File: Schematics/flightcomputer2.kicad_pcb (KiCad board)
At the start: 2 copper layers, 42 parts, among them IC1 AMS1117-3.3, J1 Pyro, J2 USB_C_Receptacle, J3 Conn_01x05_Pin, J4 Conn_Coaxial_Small, J5 Conn_01x05_Pin, J6 PyroDrogue, Q1 BSC098N10NS5, Q2 BSC098N10NS5, SW3 SW_Push, SW4 SW_Push, U2 STM32F405RGTx, U4 SN65HVD230DR

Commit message: added LCSC numbers and footprint values, need to connect schemeatic pins, then can start layout
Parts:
- removed IC1: AMS1117-3.3, Library:SOT229P700X180-4N
- removed SW3, SW4: SW_Push, Library:SAMZO G4R0015010
- added BootSwitch1: SAMZO G4R0015010, myFootprints:SAMZO G4R0015010, F.Cu at (274.1, 76.5)
- added C1: 100nf, Capacitor_SMD:C_0805_2012Metric_Pad1.18x1.45mm_HandSolder, F.Cu at (242.4, 142.0)
- added C10: 100nf, Capacitor_SMD:C_0805_2012Metric_Pad1.18x1.45mm_HandSolder, F.Cu at (42.9, 40.8)
- added C11: 100nf, Capacitor_SMD:C_0805_2012Metric_Pad1.18x1.45mm_HandSolder, F.Cu at (45.9, 40.8)
- added C12: 1u, Capacitor_SMD:C_0805_2012Metric_Pad1.18x1.45mm_HandSolder, F.Cu at (48.9, 40.8)
- added C14: 18p, Capacitor_SMD:C_0603_1608Metric_Pad1.08x0.95mm_HandSolder, F.Cu at (42.6, 75.7)
- added C16: 100nf, Capacitor_SMD:C_0805_2012Metric_Pad1.18x1.45mm_HandSolder, F.Cu at (206.3, 124.1)
- added C17: 1u, Capacitor_SMD:C_0805_2012Metric_Pad1.18x1.45mm_HandSolder, F.Cu at (97.6, 99.7)
- added C18: 33u, Capacitor_SMD:C_0805_2012Metric_Pad1.18x1.45mm_HandSolder, F.Cu at (97.6, 102.7)
- added C19: 100nf, Capacitor_SMD:C_0805_2012Metric_Pad1.18x1.45mm_HandSolder, F.Cu at (32.1, 119.1)
- added C21: 100nf, Capacitor_SMD:C_0805_2012Metric_Pad1.18x1.45mm_HandSolder, F.Cu at (28.8, 126.5)
- added C22: 100nf, Capacitor_SMD:C_0805_2012Metric_Pad1.18x1.45mm_HandSolder, F.Cu at (30.4, 48.6)
- added C23: 100nf, Capacitor_SMD:C_0805_2012Metric_Pad1.18x1.45mm_HandSolder, F.Cu at (30.4, 51.6)
- added C7: 100nf, Capacitor_SMD:C_0805_2012Metric_Pad1.18x1.45mm_HandSolder, F.Cu at (39.9, 40.8)
- added CAN_IN1: CAN, myFootprints:MOLEX_26013114, F.Cu at (19.2, 144.3)
- added CAN_OUT1: CAN, myFootprints:MOLEX_26013114, F.Cu at (28.6, 144.3)
- added D1: NeoPixel_THT, LED_SMD:LED_Kingbright_AAA3528ESGCT, F.Cu at (261.3, 148.6)
- added D3: SRV05-4.TCT, myFootprints:SOT95P280X145-6N, F.Cu at (213.8, 32.2)
- added J1: Microsemi_FlashPro-JTAG-10, myFootprints:CONN_7024610XX_MOL, F.Cu at (82.2, 34.7)
- added J7: Conn_Coaxial_Small, Connector_Coaxial:SMA_Amphenol_132291_Vertical, F.Cu at (137.4, 29.8)
- added J8: Micro_SD_Card, Connector_Card:microSD_HC_Molex_104031-0811, F.Cu at (199.7, 27.2)
- added JP1: SolderJumper_2_Open, Jumper:SolderJumper-2_P1.3mm_Open_TrianglePad1.0x1.5mm, F.Cu at (207.8, 128.9)
- added MPL3115A2R1: MPL3115A2R1, myFootprints:PSON80P300X300X100-8N, F.Cu at (36.8, 120.7)
- added PowerLED1: RLED, LED_SMD:LED_0603_1608Metric_Pad1.05x0.95mm_HandSolder, F.Cu at (263.1, 107.3)
- added R1: 10k, Resistor_SMD:R_0805_2012Metric_Pad1.20x1.40mm_HandSolder, F.Cu at (258.6, 41.5)
- added R16: 10k, Resistor_SMD:R_0805_2012Metric_Pad1.20x1.40mm_HandSolder, F.Cu at (200.7, 38.3)
- added R17: 220R, Resistor_SMD:R_0805_2012Metric_Pad1.20x1.40mm_HandSolder, F.Cu at (203.6, 38.3)
- added R2: 100k, Resistor_SMD:R_0805_2012Metric_Pad1.20x1.40mm_HandSolder, F.Cu at (267.2, 78.1)
- added R3: 1k, Resistor_SMD:R_0805_2012Metric_Pad1.20x1.40mm_HandSolder, F.Cu at (258.5, 102.0)
- added R4: 330R, Resistor_SMD:R_0805_2012Metric_Pad1.20x1.40mm_HandSolder, F.Cu at (247.2, 150.8)
- added R9: 120R, Resistor_SMD:R_0805_2012Metric_Pad1.20x1.40mm_HandSolder, F.Cu at (212.0, 124.2)
- added RSTSwitch1: SAMZO G4R0015010, myFootprints:SAMZO G4R0015010, F.Cu at (265.5, 48.5)
- added U2: SN65HVD230, Package_SO:SOIC-8_3.9x4.9mm_P1.27mm, F.Cu at (211.8, 118.0)
- added U3: AMS1117-3.3, Package_TO_SOT_SMD:SOT-223-3_TabPin2, F.Cu at (100.1, 94.1)
- added U5: H3LIS100DL, myFootprints:PQFN50P300X300X100-16N, F.Cu at (30.1, 91.7)
- added Y1: 8mhz, Crystal:Crystal_SMD_3225-4Pin_3.2x2.5mm_HandSoldering, F.Cu at (33.3, 67.0)
- C15: value 100nf -> 18p; footprint Capacitor_SMD:C_0805_2012Metric_Pad1.18x1.45mm_HandSolder -> Capacitor_SMD:C_0603_1608Metric_Pad1.08x0.95mm_HandSolder
- C9: renamed from C12; value 10u -> 100nf
- D2: footprint Library:SOT95P280X145-6N -> myFootprints:SOT95P280X145-6N
- J2: renamed from J6; value PyroDrogue -> Pyro; footprint Connector_Molex:Molex_KK-254_AE-6410-02A_1x02_P2.54mm_Vertical -> myFootprints:MOLEX_26013114
- J4: renamed from J1; footprint Connector_Molex:Molex_KK-254_AE-6410-02A_1x02_P2.54mm_Vertical -> myFootprints:MOLEX_26013114
- Q1: renamed from Q2; footprint Package_TO_SOT_SMD:SOT-23 -> Package_TO_SOT_SMD:SOT-23-5
- Q2: renamed from Q1; footprint Package_TO_SOT_SMD:SOT-23 -> Package_TO_SOT_SMD:SOT-23-5
- R12: renamed from R9; footprint Resistor_SMD:R_0805_2012Metric -> Resistor_SMD:R_0805_2012Metric_Pad1.20x1.40mm_HandSolder
- R7: renamed from R11; footprint Resistor_SMD:R_0805_2012Metric -> Resistor_SMD:R_0805_2012Metric_Pad1.20x1.40mm_HandSolder
- U1: renamed from U2; value STM32F405RGTx -> STM32F405RGT6
- U4: value SN65HVD230DR -> LSM6DS3TR-C; footprint Library:SOIC127P599X175-8N -> myFootprints:LGA-14-2.5X3MM
- moved R6 188.3 mm to (52.1, 169.0)
- moved R6 188.3 mm to (59.4, 157.5)
- moved R7 188.3 mm to (59.4, 148.7)
- moved R5 188.3 mm to (59.4, 154.6)
- moved R5 188.3 mm to (52.1, 166.1)
- moved R7 188.3 mm to (59.5, 173.0)
- moved R8 188.3 mm to (59.4, 151.6)
- moved R8 188.3 mm to (59.5, 185.2)
- moved R10 177.2 mm to (115.4, 174.4)
- moved R11 177.2 mm to (115.4, 177.3)
- moved R13 177.2 mm to (115.4, 183.2)
- moved R12 177.2 mm to (115.4, 180.3)
- moved C20 175.8 mm to (33.6, 126.9)
- moved C15 158.4 mm to (27.9, 75.1)
- moved C13 155.7 mm to (34.0, 25.1)
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- renumbered C17 to C13, C3 to C2, C13 to C3, C14 to C4, C18 to C5, C19 to C6, C11 to C8, FB2 to FB1, J2 to J3, J3 to J5, J5 to J6, R1 to R10, R2 to R11, R10 to R13, R3 to R14, R4 to R15, R13 to R5, R14 to R6, R12 to R8
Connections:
- net vbat renamed +BATT
- C13 pad 1: +3.3V -> +3.3VA
- C13 pad 2: GND -> +3.3V
- C15 pad 1: +3.3V -> /MCU/OSC OUT
- C15 pad 2: GND -> +3.3V
- C2 pad 1: /MCU1/NRST -> /MCU/NRST
- C20 pad 2: GND -> +3.3V
- C3 pad 2: GND -> +3.3V
- C4 pad 2: GND -> +3.3V
- C5 pad 2: GND -> +3.3V
- C6 pad 2: GND -> +3.3V
- C8 pad 1: GND -> +3.3V
- C8 pad 2: +3.3VA -> +3.3V
- C9 pad 1: GND -> +3.3V
- CBulk1 pad 2: GND -> +3.3V
- D2 pad 2: GND -> +3.3V
- D2 pad 5: VBUS -> +5V
- J2 pad 2: Net-(J6-Pin_2) -> Net-(J2-Pin_2)
- J3 pad S1: GND -> +3.3V
- J4 pad 2: Net-(J1-Pin_2) -> Net-(J4-Pin_2)
- J5 pad 2: GND -> +3.3V
- J5 pad 4: Net-(J3-Pin_4) -> GPS1_RX
- J6 pad 2: GND -> +3.3V
- J6 pad 4: Net-(J5-Pin_4) -> GPS2_RX
- Q1 pad 1: GND -> +3.3V
- Q1 pad 2: GND -> +3.3V
- Q1 pad 3: GND -> +3.3V
- Q2 pad 1: GND -> +3.3V
- Q2 pad 2: GND -> +3.3V
- Q2 pad 3: GND -> +3.3V
- R10 pad 1: Net-(Q1-G) -> Net-(Q2-G)
- R10 pad 2: PA9 -> /Drogue/DrougeIgnite
- R11 pad 1: Net-(Q1-G) -> Net-(Q2-G)
- R11 pad 2: GND -> +3.3V
- R12 pad 1: Net-(J1-Pin_2) -> Net-(J4-Pin_2)
- R12 pad 2: PA3 -> /Drogue/DrougeACD
- R13 pad 1: PA3 -> /Drogue/DrougeACD
- R13 pad 2: GND -> +3.3V
- R14 pad 2: GND -> +3.3V
- R15 pad 2: GND -> +3.3V
- R5 pad 1: Net-(Q2-G) -> Net-(Q1-G)
- R5 pad 2: PA8 -> /Pyro/PyroIgnite
- R6 pad 1: Net-(Q2-G) -> Net-(Q1-G)
- R6 pad 2: GND -> +3.3V
- R7 pad 1: Net-(J6-Pin_2) -> Net-(J2-Pin_2)
- R7 pad 2: PA3 -> /Pyro/PyroADC
- R8 pad 1: PA3 -> /Pyro/PyroADC
- R8 pad 2: GND -> +3.3V
- U1 pad 10: unconnected-(U2-PC2-Pad10) -> /MCU/SPI2-MISO
- U1 pad 11: unconnected-(U2-PC3-Pad11) -> /MCU/SPI2-MOSI
- U1 pad 12: GND -> +3.3V
- U1 pad 13: +3.3V -> +3.3VA
- U1 pad 15: unconnected-(U2-PA1-Pad15) -> /MCU/PyroADC
- U1 pad 17: PA3 -> unconnected-(U1-PA3-Pad17)
- U1 pad 18: GND -> +3.3V
- U1 pad 24: unconnected-(U2-PC4-Pad24) -> /MCU/RGB_DATA
- U1 pad 25: unconnected-(U2-PC5-Pad25) -> /MCU/DrougeADC
- U1 pad 29: GPS1_TX -> /MCU/GPS1_TX
- U1 pad 30: GPS1_RX -> /MCU/GPS1_RX
- U1 pad 33: CAN_RX_2 -> /MCU/CAN_RX_2
- U1 pad 34: CAN_TX_2 -> /MCU/CAN_TX_2
- U1 pad 37: GPS2_RX -> /MCU/GPS2_RX
- U1 pad 38: GPS2_TX -> /MCU/GPS2_TX
- U1 pad 41: PA8 -> unconnected-(U1-PA8-Pad41)
- U1 pad 42: PA9 -> /MCU/VBUS
- U1 pad 44: D- -> /MCU/D-
- U1 pad 45: D+ -> /MCU/D+
- U1 pad 46: VBUS -> /MCU/SWDIO
- U1 pad 49: unconnected-(U2-PA14-Pad49) -> /MCU/SWCLK
- U1 pad 5: unconnected-(U2-PH0-Pad5) -> /MCU/OSC IN
- U1 pad 53: UART_DEBUG_TX -> unconnected-(U1-PC12-Pad53)
- U1 pad 54: UART_DEBUG_RX -> unconnected-(U1-PD2-Pad54)
- U1 pad 58: unconnected-(U2-PB6-Pad58) -> /MCU/I2CSDA
- U1 pad 59: unconnected-(U2-PB7-Pad59) -> /MCU/I2CSDL
- U1 pad 6: unconnected-(U2-PH1-Pad6) -> /MCU/OSC OUT
- U1 pad 60: /MCU1/BOOT0 -> /MCU/BOOT0
- U1 pad 63: GND -> +3.3V
- U1 pad 7: /MCU1/NRST -> /MCU/NRST
- U4 pad 1: CAN_TX_2 -> +3.3V
- U4 pad 2: GND -> +3.3V
- U4 pad 3: +3V3 -> +3.3V
- U4 pad 4: CAN_RX_2 -> unconnected-(U4-INT1-Pad4)
- U4 pad 5: unconnected-(U4-VREF-Pad5) -> +3.3V
- U4 pad 6: CANL -> +3.3V
- U4 pad 7: CANH -> +3.3V
- U4 pad 8: GND -> +3.3V

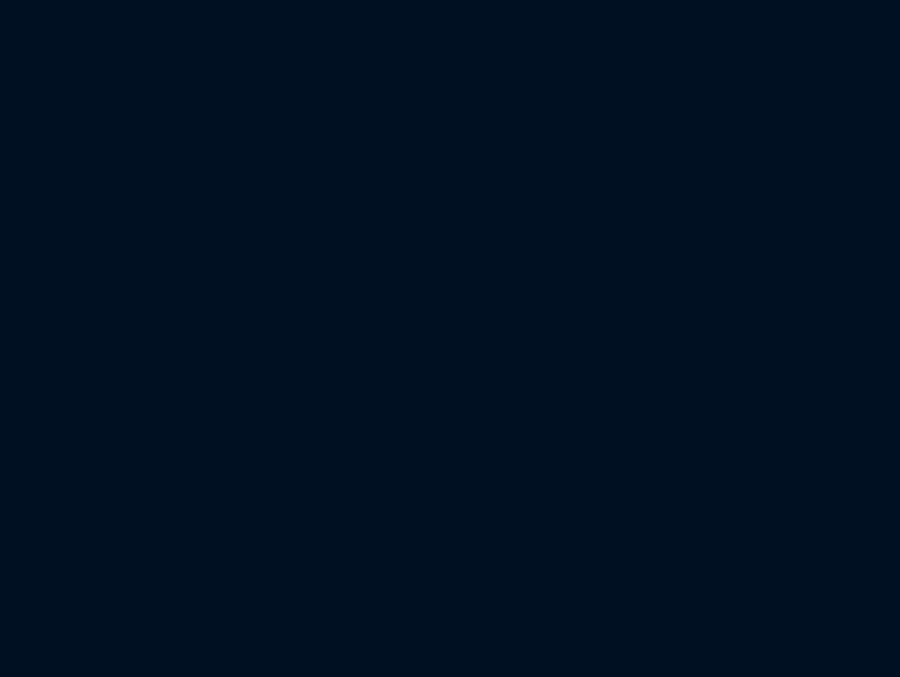
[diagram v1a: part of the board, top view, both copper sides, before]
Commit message: started lora schematic all pcb parts should be included
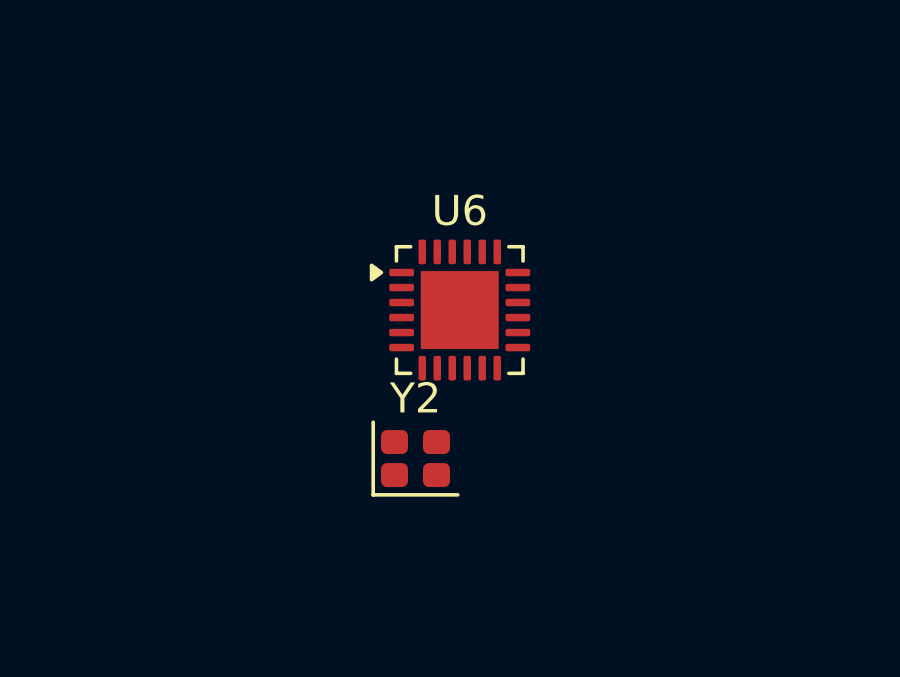
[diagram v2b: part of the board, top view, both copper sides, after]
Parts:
- added U6: SX1262IMLTRT, Package_DFN_QFN:QFN-24-1EP_4x4mm_P0.5mm_EP2.6x2.6mm, F.Cu at (139.1, 118.6)
- added Y2: Crystal_GND24, Crystal:Crystal_SMD_2016-4Pin_2.0x1.6mm, F.Cu at (137.6, 123.5)

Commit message: finished pin assignments and ran ERC all good ready for layout
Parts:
- removed the C2 at (268.2, 39.9)
- removed the C2 at (275.3, 47.0)
- removed CBulk1: 4.7u, Capacitor_SMD:C_0805_2012Metric_Pad1.18x1.45mm_HandSolder
- removed the R4 at (247.2, 150.8)
- removed the R8 at (59.5, 185.2)
- removed the U6 at (139.1, 118.6)
- removed Y2: Crystal_GND24, Crystal:Crystal_SMD_2016-4Pin_2.0x1.6mm
- added C2: 100nf, Capacitor_SMD:C_0805_2012Metric_Pad1.18x1.45mm_HandSolder, F.Cu at (144.9, 96.1)
- added C23: 100nf, Capacitor_SMD:C_0805_2012Metric_Pad1.18x1.45mm_HandSolder, F.Cu at (128.3, 66.5)
- added C26: 100nf, Capacitor_SMD:C_0805_2012Metric_Pad1.18x1.45mm_HandSolder, F.Cu at (105.0, 97.0)
- added C27: 1u, Capacitor_SMD:C_0805_2012Metric_Pad1.18x1.45mm_HandSolder, F.Cu at (105.0, 100.0)
- added C8: 4.7u, Capacitor_SMD:C_0805_2012Metric_Pad1.18x1.45mm_HandSolder, F.Cu at (126.5, 87.6)
- added D2: D_Schottky, Diode_SMD:D_2114_3652Metric, F.Cu at (121.4, 123.3)
- added D3: D_Schottky, Diode_SMD:D_2114_3652Metric, F.Cu at (121.5, 118.5)
- added U4: RFM95W-915S2, myFootprints:XCVR_RFM95W-915S2, F.Cu at (111.0, 139.0)
- C15: renamed from C14; footprint Capacitor_SMD:C_0603_1608Metric_Pad1.08x0.95mm_HandSolder -> Capacitor_SMD:C_0805_2012Metric_Pad1.18x1.45mm_HandSolder
- C16: renamed from C15; footprint Capacitor_SMD:C_0603_1608Metric_Pad1.08x0.95mm_HandSolder -> Capacitor_SMD:C_0805_2012Metric_Pad1.18x1.45mm_HandSolder
- C19: renamed from C18; value 33u -> 4.7u
- J8: footprint Connector_Card:microSD_HC_Molex_104031-0811 -> Connector_Card:microSD_HC_Molex_47219-2001
- U3: value AMS1117-3.3 -> LDL1117-3.3; footprint Package_TO_SOT_SMD:SOT-223-3_TabPin2 -> myFootprints:SOT230P700X180-4N
- U5: renamed from MPL3115A2R1; footprint myFootprints:PSON80P300X300X100-8N -> Package_LGA:LGA-8_3x5mm_P1.25mm
- moved CAN_IN1 152.7 mm to (134.2, 43.9), turned to 180 degrees
- moved C1 147.5 mm to (132.9, 116.7)
- moved R1 139.7 mm to (129.9, 95.7), turned to 180 degrees
- moved CAN_OUT1 139.1 mm to (124.8, 43.9), turned to 180 degrees
- moved BootSwitch1 138.4 mm to (138.2, 102.7)
- moved RSTSwitch1 135.8 mm to (138.3, 96.1)
- moved R2 129.9 mm to (140.5, 106.4)
- moved J2 128.6 mm to (146.8, 150.1)
- moved D1 127.7 mm to (138.3, 114.4)
- moved Q1 122.8 mm to (163.5, 149.7)
- moved R5 122.3 mm to (173.8, 153.8)
- moved R6 122.3 mm to (173.8, 156.8)
- moved R7 122.3 mm to (181.3, 160.7)
- moved PowerLED1 118.6 mm to (145.1, 118.7)
- moved J7 115.0 mm to (124.0, 144.0)
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- renumbered C9 to C10, C10 to C11, C11 to C12, C12 to C13, C13 to C14, C16 to C17, C17 to C18, C19 to C20, C20 to C21, C21 to C22, C22 to C24, C23 to C25, C8 to C9, D2 to D4, D3 to D5, R11 to R10, R12 to R11, R13 to R12, R14 to R13, R15 to R14, R16 to R15, R17 to R16, R5 to R4, R6 to R5, R8 to R6, R9 to R8, R10 to R9, U4 to U6, U5 to U7
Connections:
- C1 pad 1: +3.3V -> GND
- C10 pad 1: +3.3V -> GND
- C11 pad 2: +3.3V -> GND
- C12 pad 2: +3.3V -> GND
- C13 pad 2: +3.3V -> GND
- C14 pad 2: +3.3V -> GND
- C15 pad 2: +3.3V -> GND
- C16 pad 2: +3.3V -> GND
- C17 pad 2: +3.3V -> GND
- C18 pad 1: +BATT -> Net-(D2-K)
- C18 pad 2: +3.3V -> GND
- C19 pad 2: +3.3V -> GND
- C20 pad 2: +3.3V -> GND
- C21 pad 2: +3.3V -> GND
- C22 pad 2: +3.3V -> GND
- C24 pad 2: +3.3V -> GND
- C25 pad 2: +3.3V -> GND
- C3 pad 2: +3.3V -> GND
- C4 pad 2: +3.3V -> GND
- C5 pad 2: +3.3V -> GND
- C6 pad 2: +3.3V -> GND
- C7 pad 2: +3.3V -> GND
- C9 pad 1: +3.3V -> GND
- D1 pad 2: +3.3V -> GND
- D1 pad 4: Net-(D1-DIN) -> /MCU/RGB_DATA
- D4 pad 1: D+ -> /MCU/D+
- D4 pad 2: +3.3V -> GND
- D4 pad 3: D- -> /MCU/D-
- D5 pad 2: +3.3V -> GND
- J1 pad 10: +3.3V -> GND
- J1 pad 2: +3.3V -> GND
- J3 pad A6: D+ -> /MCU/D+
- J3 pad A7: D- -> /MCU/D-
- J3 pad B6: D+ -> /MCU/D+
- J3 pad B7: D- -> /MCU/D-
- J3 pad S1: +3.3V -> GND
- J5 pad 2: +3.3V -> GND
- J5 pad 3: GPS1_TX -> /GPS/GPS1_TX
- J5 pad 4: GPS1_RX -> /GPS/GPS1_RX
- J5 pad 5: RESET -> /GPS/RESET1
- J7 pad 1: unconnected-(J7-In-Pad1) -> Net-(J7-In)
- J7 pad 2: +3.3V -> GND
- J8 pad 6: +3.3V -> GND
- J8 pad 9: +3.3V -> GND
- PowerLED1 pad 1: +3.3V -> GND
- Q1 pad 1: +3.3V -> GND
- Q1 pad 2: +3.3V -> GND
- Q1 pad 3: +3.3V -> GND
- Q2 pad 1: +3.3V -> GND
- Q2 pad 2: +3.3V -> GND
- Q2 pad 3: +3.3V -> GND
- R10 pad 2: +3.3V -> GND
- R11 pad 1: Net-(J4-Pin_2) -> /Drogue/DrougeADC
- R11 pad 2: /Drogue/DrougeACD -> Net-(J4-Pin_2)
- R12 pad 1: /Drogue/DrougeACD -> /Drogue/DrougeADC
- R12 pad 2: +3.3V -> GND
- R13 pad 2: +3.3V -> GND
- R14 pad 2: +3.3V -> GND
- R2 pad 1: +3.3V -> GND
- R4 pad 2: /Pyro/PyroIgnite -> /MCU/PyroIgnite
- R5 pad 2: +3.3V -> GND
- R6 pad 1: /Pyro/PyroADC -> /MCU/PyroADC
- R6 pad 2: +3.3V -> Net-(J2-Pin_2)
- R7 pad 1: Net-(J2-Pin_2) -> GND
- R7 pad 2: /Pyro/PyroADC -> /MCU/PyroADC
- RSTSwitch1 pad 3: +3.3V -> GND
- U1 pad 10: /MCU/SPI2-MISO -> /LoRa/sxMIS0
- U1 pad 11: /MCU/SPI2-MOSI -> /LoRa/sxMOSI
- U1 pad 12: +3.3V -> GND
- U1 pad 14: unconnected-(U1-PA0-Pad14) -> /GPS/GPS1_RX
- U1 pad 18: +3.3V -> GND
- U1 pad 21: unconnected-(U1-PA5-Pad21) -> /FlashSd/SDMOSI
- U1 pad 22: unconnected-(U1-PA6-Pad22) -> /FlashSd/SDCLK
- U1 pad 23: unconnected-(U1-PA7-Pad23) -> /FlashSd/SDMISO
- U1 pad 25: /MCU/DrougeADC -> /Drogue/DrougeADC
- U1 pad 29: /MCU/GPS1_TX -> /LoRa/sxSCK
- U1 pad 30: /MCU/GPS1_RX -> unconnected-(U1-PB11-Pad30)
- U1 pad 33: /MCU/CAN_RX_2 -> /Can_transceiver/CAN_TX_2
- U1 pad 34: /MCU/CAN_TX_2 -> /Can_transceiver/CAN_RX_2
- U1 pad 36: unconnected-(U1-PB15-Pad36) -> /MCU/PyroIgnite
- U1 pad 37: /MCU/GPS2_RX -> /Drogue/DrougeIgnite
- U1 pad 38: /MCU/GPS2_TX -> unconnected-(U1-PC7-Pad38)
- U1 pad 40: unconnected-(U1-PC9-Pad40) -> /GPS/RESET2
- U1 pad 41: unconnected-(U1-PA8-Pad41) -> /GPS/RESET1
- U1 pad 42: /MCU/VBUS -> +5V
- U1 pad 52: unconnected-(U1-PC11-Pad52) -> /GPS/GPS1_TX
- U1 pad 53: unconnected-(U1-PC12-Pad53) -> /GPS/GPS2_RX
- U1 pad 54: unconnected-(U1-PD2-Pad54) -> /GPS/GPS2_TX
- U1 pad 55: unconnected-(U1-PB3-Pad55) -> /LoRa/sxReset
- U1 pad 56: unconnected-(U1-PB4-Pad56) -> /LoRa/sxNSS
- U1 pad 57: unconnected-(U1-PB5-Pad57) -> /LoRa/sxDIO1
- U1 pad 58: /MCU/I2CSDA -> /Accelerometer/AccelerometerSCL
- U1 pad 59: /MCU/I2CSDL -> /Accelerometer/AccelerometerSDA
- U1 pad 63: +3.3V -> GND
- U2 pad 2: +3.3V -> GND
- U2 pad 8: +3.3V -> GND
- U3 pad 1: +3.3V -> Net-(D2-K)
- U3 pad 2: +3.3V -> GND
- U3 pad 3: +BATT -> +3.3V
- U5 pad 3: +3.3V -> GND
- U5 pad 7: /Barometer/BarometerSDL -> /Accelerometer/AccelerometerSDA
- U5 pad 8: /Barometer/BarometerSCL -> /Accelerometer/AccelerometerSCL
- U6 pad 1: +3.3V -> GND
- U6 pad 13: /IMU/IMUSCL -> /Accelerometer/AccelerometerSCL
- U6 pad 14: /IMU/IMUSCL -> /Accelerometer/AccelerometerSDA
- U6 pad 2: +3.3V -> GND
- U6 pad 3: +3.3V -> GND
- U6 pad 6: +3.3V -> GND
- U6 pad 7: +3.3V -> GND
- U7 pad 10: +3.3V -> unconnected-(U7-GND-Pad10)
- U7 pad 12: +3.3V -> GND
- U7 pad 13: +3.3V -> (no net)
- U7 pad 16: +3.3V -> (no net)
- U7 pad 5: +3.3V -> GND
- U7 pad 7: +3.3V -> unconnected-(U7-SDO/SA0-Pad7)
- Y1 pad 2: +3.3V -> GND
- Y1 pad 4: +3.3V -> GND
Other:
- board outline added: 50 x 100 mm
- copper layers 2 -> 4

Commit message: finalizing layout
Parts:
- added C28: 100nF, Capacitor_SMD:C_0201_0603Metric, F.Cu at (160.0, 92.2)
- added U8: W25Q128JVP, Package_SON:WSON-8-1EP_6x5mm_P1.27mm_EP3.4x4.3mm, F.Cu at (160.0, 87.0)
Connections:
- U1 pad 26: unconnected-(U1-PB0-Pad26) -> /LoRa/sxNSS
- U1 pad 27: unconnected-(U1-PB1-Pad27) -> /LoRa/sxDIO1
- U1 pad 28: unconnected-(U1-PB2-Pad28) -> /LoRa/sxReset
- U1 pad 51: unconnected-(U1-PC10-Pad51) -> /FlashMemory/SPICLK
- U1 pad 55: /LoRa/sxReset -> unconnected-(U1-PB3-Pad55)
- U1 pad 56: /LoRa/sxNSS -> /FlashMemory/SPI_MOSI
- U1 pad 57: /LoRa/sxDIO1 -> /FlashMemory/SPI_MISO
- U1 pad 8: unconnected-(U1-PC0-Pad8) -> /FlashMemory/ChipSelectFLash
